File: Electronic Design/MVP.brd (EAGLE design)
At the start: 94.6 x 78.5 mm, 36 parts, among them IC1 ACS712ELC-5A, IC3 ATMEGA328-PU, Q2 16MHz, Q3 IRF9540, Q4 IRF9540

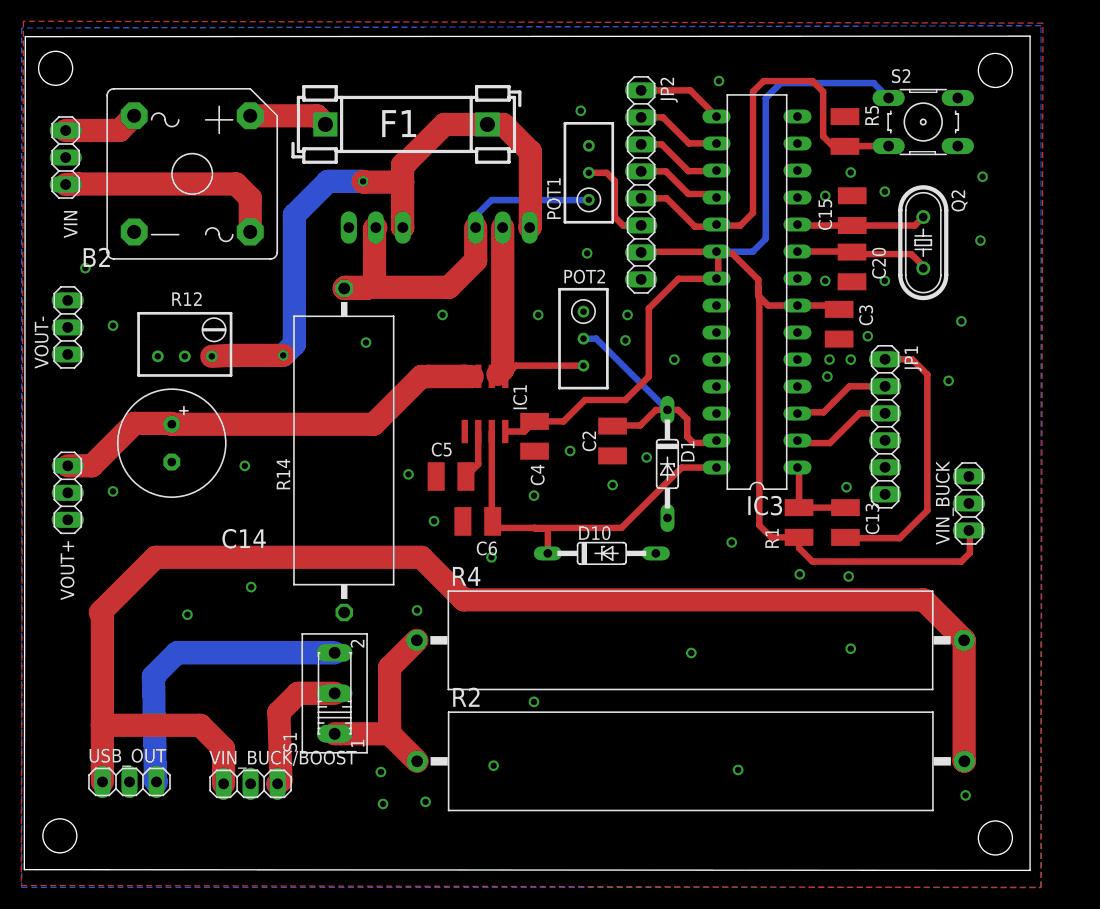
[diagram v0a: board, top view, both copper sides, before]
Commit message: changing component names so the make sense again
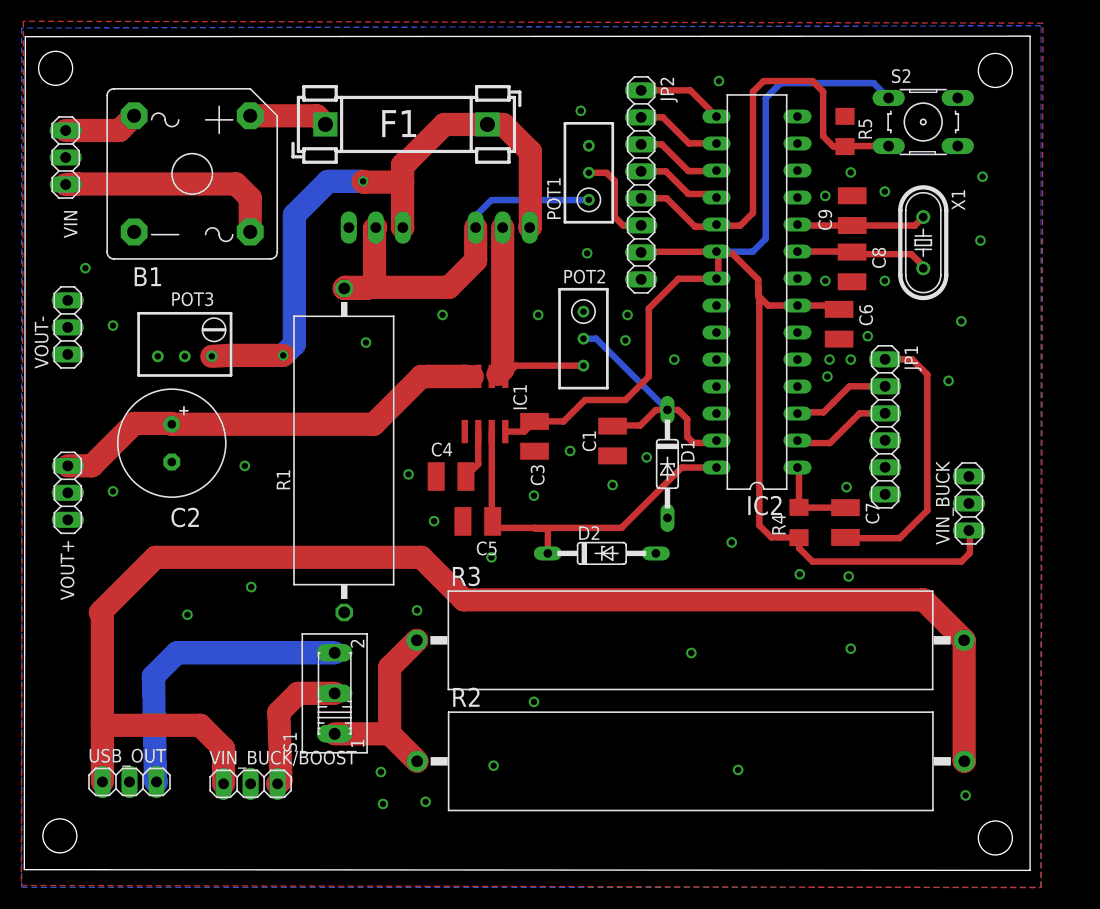
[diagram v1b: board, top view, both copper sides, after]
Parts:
- removed C14: ECA2DHG221, resistor:E3,5-10
- removed Q4: IRF9540, transistor-power:TO220BV
- removed R14: 1k, resistor:VTA52
- added C1: 10n, resistor:C1210
- added R3: 22R, resistor-power:RWM8X45
- added X1: 16MHz, crystal:HC49/S
- C2: value 10n -> ECA2DHG221; device resistor:C1210 -> resistor:E3,5-10
- C3: value 10u -> 0.1u
- C4: value 0.1u -> 1n
- C5: value 1n -> 10u
- Q2: value 16MHz -> IRF9540; device crystal:HC49/S -> transistor-power:TO220BV
- R1: value 10k -> 1k; device resistor:R1210 -> resistor:VTA52
- R4: value 22R -> 10k; device resistor-power:RWM8X45 -> resistor:R1206
- R5: device resistor:R1210 -> resistor:R1206
- moved R1 43.3 mm to (30.7, 42.7)
- moved C2 41.5 mm to (14.5, 43.3)
- moved Q2 39.6 mm to (45.7, 61.1), flipped to the bottom, turned to 180 degrees
- moved C6 38.7 mm to (77.3, 54.5), turned to 270 degrees
- moved C3 30.5 mm to (48.7, 44.0)
- moved R4 15.1 mm to (73.5, 35.9), turned to 90 degrees
- moved C4 8.72 mm to (40.8, 40.2), turned to 0 degrees
- moved C5 4.92 mm to (43.3, 36.0), turned to 180 degrees
- renumbered B2 to B1, C13 to C7, C15 to C9, C20 to C8, D10 to D2, IC3 to IC2, Q3 to Q1, R12 to POT3
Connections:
- net +5V: now also C6.1, R4.1; no longer C4.1, R1.1
- net GND: now also C1.2, C2.-, C4.1, C5.2, R1.1; no longer C14.-, C2.2, C4.2, C5.1, R14.1
- net IIN: now also C5.1; no longer C6.1
- net M1S: now also C2.+; no longer C14.+
- net N$10: now also Q2.S; no longer Q4.S
- net N$15: now also X1.1; no longer Q2.1
- net N$16: now also X1.2; no longer Q2.2
- net N$17: now also R4.2; no longer R1.2
- net N$2: now also C4.2; no longer C5.2
- net N$23: now also R3.2; no longer R4.2
- net N$24: now also R3.1; no longer R4.1
- net N$3: now also Q2.D; no longer Q4.D
- net N$35: now also Q2.G, R1.2; no longer Q4.G, R14.2
- net VIN: now also C1.1; no longer C2.1

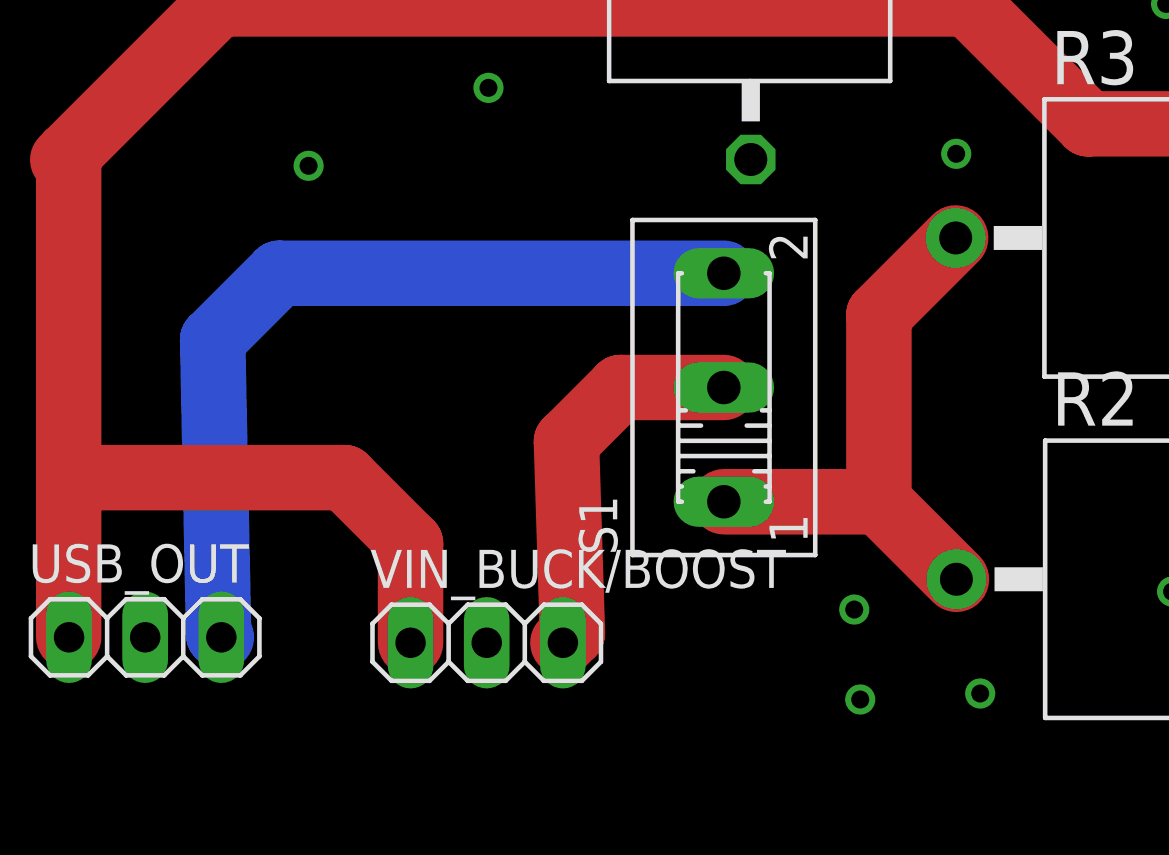
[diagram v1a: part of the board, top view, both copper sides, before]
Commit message: replacing switch on PCB with pin header as originally intended
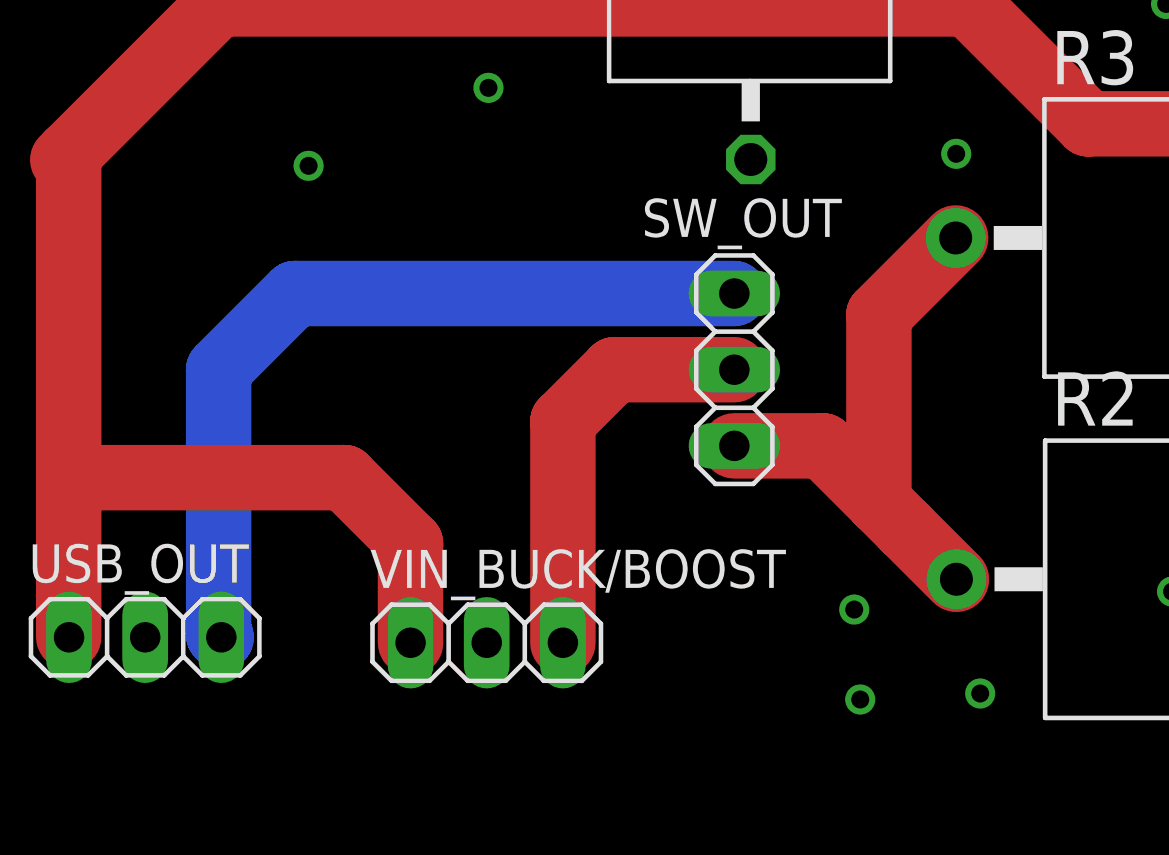
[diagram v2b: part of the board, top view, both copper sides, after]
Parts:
- removed S1: (no value), switch:255SB
- added SW_OUT: (no value), pinhead:1X03
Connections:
- net N$22: now also SW_OUT.2; no longer S1.2
- net N$24: now also SW_OUT.3; no longer S1.1
- net N$25: now also SW_OUT.1; no longer S1.3
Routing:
- net N$22: track 12.8 -> 13.8 mm
- net N$25: track 27.9 -> 27.2 mm
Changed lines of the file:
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@@
 <attribute name="MPN" value="" x="63.32248125" y="24.793921875" size="1.778" layer="27" display="off"/>
 </element>
-<element name="S1" library="switch" package="255SB" value="" x="29.850796875" y="19.80604375" rot="R90"/>
 <element name="USB_OUT" library="pinhead" package="1X03" value="" x="10.550340625" y="11.474365625"/>
 <element name="S2" library="switch-omron" package="B3F-10XX" value="" x="85.21319375" y="73.54805625">
@@
 <element name="C5" library="resistor" package="C1210" value="10u" x="43.3164375" y="35.976203125" rot="R180"/>
 <element name="C4" library="resistor" package="C1210" value="1n" x="40.8" y="40.2"/>
+<element name="SW_OUT" library="pinhead" package="1X03" value="" x="30.2" y="20.4" smashed="yes" rot="R270">
+<attribute name="NAME" x="27.1138" y="24.8288" size="1.27" layer="25" ratio="10"/>
+<attribute name="VALUE" x="27.025" y="24.21" size="1.27" layer="27" rot="R270"/>
+</element>
 </elements>
 <signals>
@@
 </signal>
 <signal name="N$22">
-<contactref element="S1" pad="2"/>
 <contactref element="VIN_BUCK/BOOST" pad="3"/>
-<wire x1="29.850796875" y1="19.80604375" x2="26.40604375" y2="19.80604375" width="2.1844" layer="1"/>
-<wire x1="26.40604375" y1="19.80604375" x2="24.6" y2="18" width="2.1844" layer="1"/>
-<wire x1="24.6" y1="18" x2="24.8" y2="11.611225" width="2.1844" layer="1"/>
-<wire x1="24.8" y1="11.611225" x2="24.48176875" y2="11.29299375" width="2.1844" layer="1"/>
+<contactref element="SW_OUT" pad="2"/>
+<wire x1="24.48176875" y1="11.29299375" x2="24.48176875" y2="18.68176875" width="2.1844" layer="1"/>
+<wire x1="24.48176875" y1="18.68176875" x2="26.2" y2="20.4" width="2.1844" layer="1"/>
+<wire x1="26.2" y1="20.4" x2="30.2" y2="20.4" width="2.1844" layer="1"/>
 </signal>
 <signal name="N$23">
@@
 <contactref element="R2" pad="1"/>
 <contactref element="R3" pad="1"/>
-<contactref element="S1" pad="1"/>
-<wire x1="29.850796875" y1="15.99604375" x2="35.021509375" y2="15.99604375" width="2.1844" layer="1"/>
-<wire x1="35.021509375" y1="15.99604375" x2="37.60721875" y2="13.410334375" width="2.1844" layer="1"/>
+<wire x1="35.021509375" y1="15.99604375" x2="35.908778125" y2="15.108775" width="2.1844" layer="1"/>
+<wire x1="35.908778125" y1="15.108775" x2="37.60721875" y2="13.410334375" width="2.1844" layer="1"/>
 <wire x1="35.021509375" y1="15.99604375" x2="35.021509375" y2="22.23295" width="2.1844" layer="1"/>
 <wire x1="35.021509375" y1="22.23295" x2="37.58248125" y2="24.793921875" width="2.1844" layer="1"/>
+<contactref element="SW_OUT" pad="3"/>
+<wire x1="30.2" y1="17.86" x2="33.157553125" y2="17.86" width="2.1844" layer="1"/>
+<wire x1="33.157553125" y1="17.86" x2="35.021509375" y2="15.99604375" width="2.1844" layer="1"/>
 </signal>
 <signal name="N$25">
 <contactref element="USB_OUT" pad="3"/>
-<contactref element="S1" pad="3"/>
-<wire x1="29.850796875" y1="23.61604375" x2="15.01604375" y2="23.61604375" width="2.1844" layer="16"/>
-<wire x1="15.01604375" y1="23.61604375" x2="12.8" y2="21.4" width="2.1844" layer="16"/>
-<wire x1="12.8" y1="21.4" x2="13" y2="11.56470625" width="2.1844" layer="16"/>
+<contactref element="SW_OUT" pad="1"/>
+<wire x1="30.2" y1="22.94" x2="15.54" y2="22.94" width="2.1844" layer="16"/>
+<wire x1="15.54" y1="22.94" x2="13" y2="20.4" width="2.1844" layer="16"/>
+<wire x1="13" y1="20.4" x2="13" y2="11.56470625" width="2.1844" layer="16"/>
 <wire x1="13" y1="11.56470625" x2="13.090340625" y2="11.474365625" width="2.1844" layer="16"/>
 </signal>

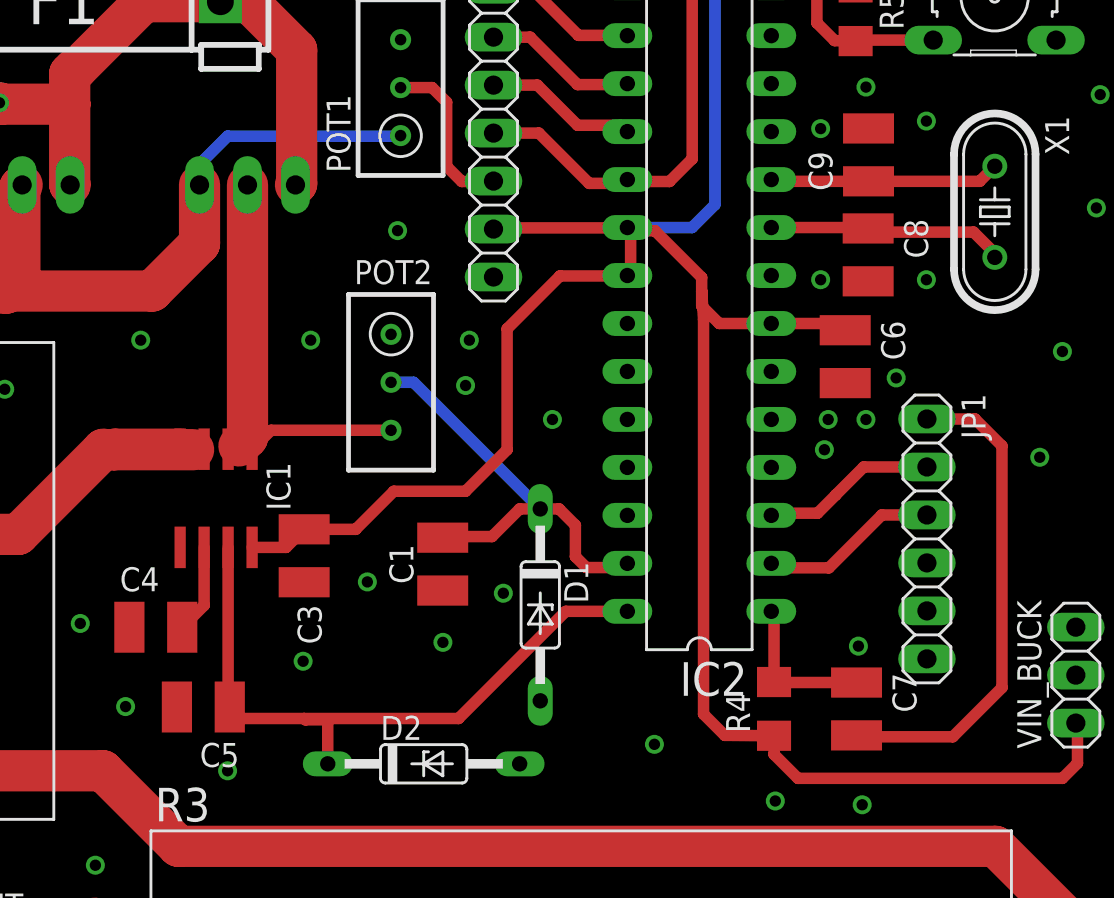
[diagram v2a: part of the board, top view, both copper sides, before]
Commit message: changing all caps and resistors to correct size
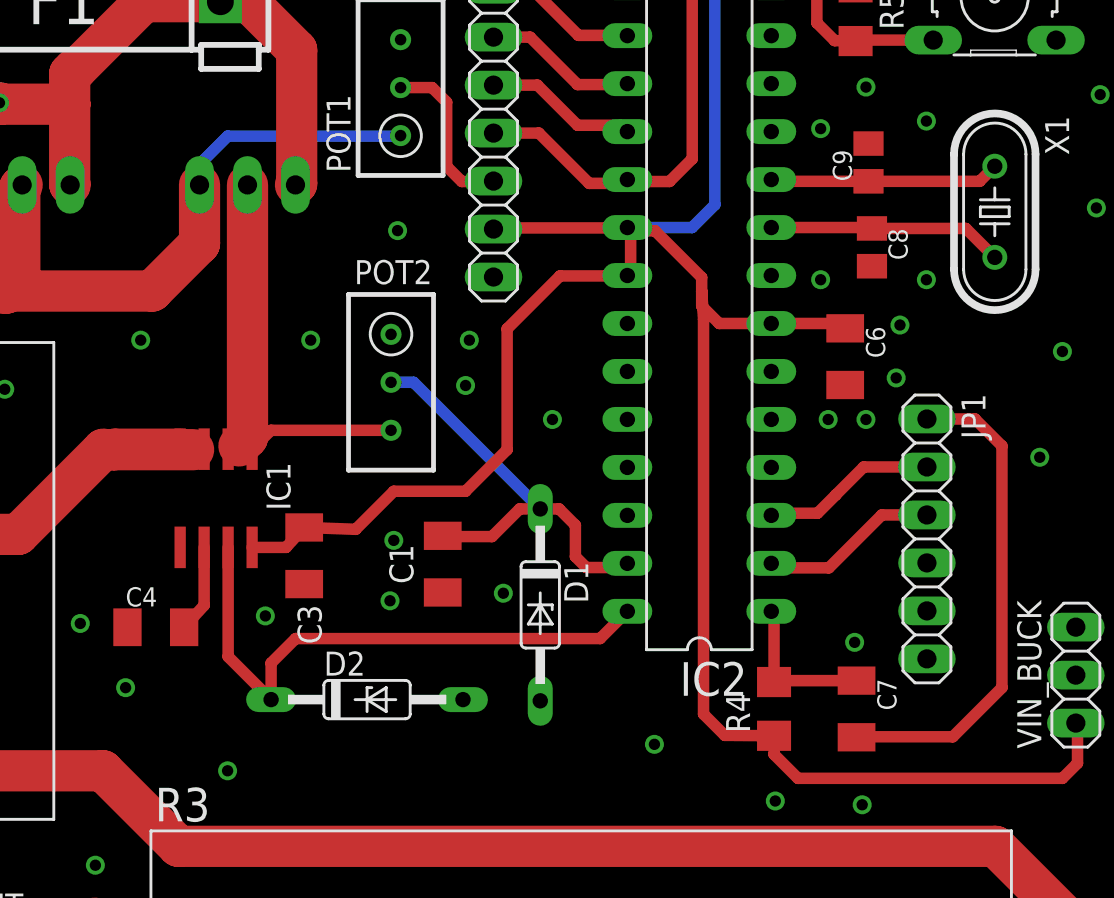
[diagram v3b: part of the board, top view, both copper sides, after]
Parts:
- removed C5: 10u, resistor:C1210
- C1, C3, C6: device resistor:C1210 -> resistor:C1206K
- C4: value 1n -> 0.1u; device resistor:C1210 -> resistor:C1206K
- C7: value 100n -> 0.1u; device resistor:C1210 -> resistor:C1206K
- C8, C9: device resistor:C1210 -> resistor:C0805K
- moved D2 4.53 mm to (52.0, 36.4)
- moved C8 0.45 mm to (78.7, 60.3)
- moved C9 0.40 mm to (78.5, 64.8)
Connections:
- net GND: no longer C5.2
- net IIN: no longer C5.1
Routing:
- net IIN: track 35.8 -> 30.9 mm
- net N$16: track 12.6 -> 13.1 mm
